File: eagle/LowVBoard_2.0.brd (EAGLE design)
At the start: 113 x 45.7 mm, 33 parts, among them IC1 ATMEGA328P-PU, IC2 MCP7940M, IC3 SN74HC595, IC4 SN74HC595, J1 CONNJACKR/APCB5.5X2.1MM, Q1 16MHz, Q2 32.768kHz

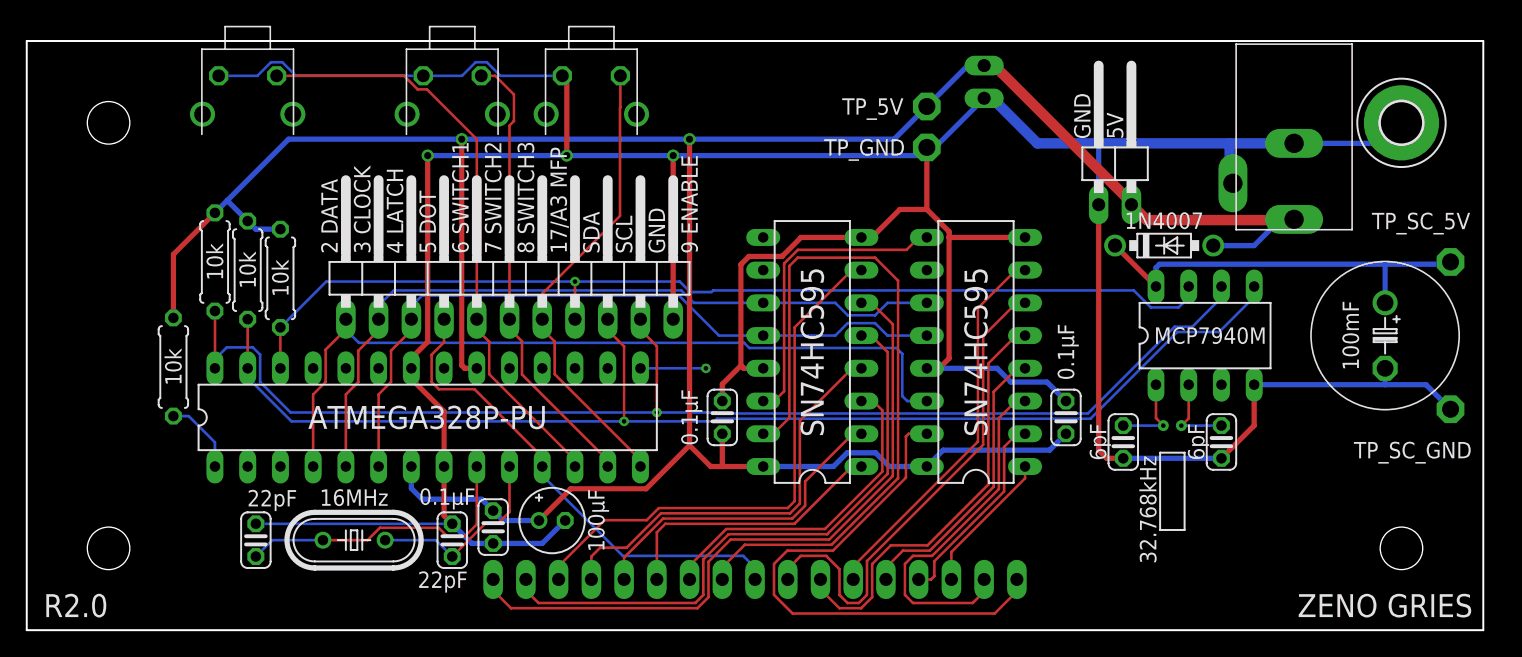
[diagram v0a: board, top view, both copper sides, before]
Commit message: added clearance for wodden board in front of switches and jack
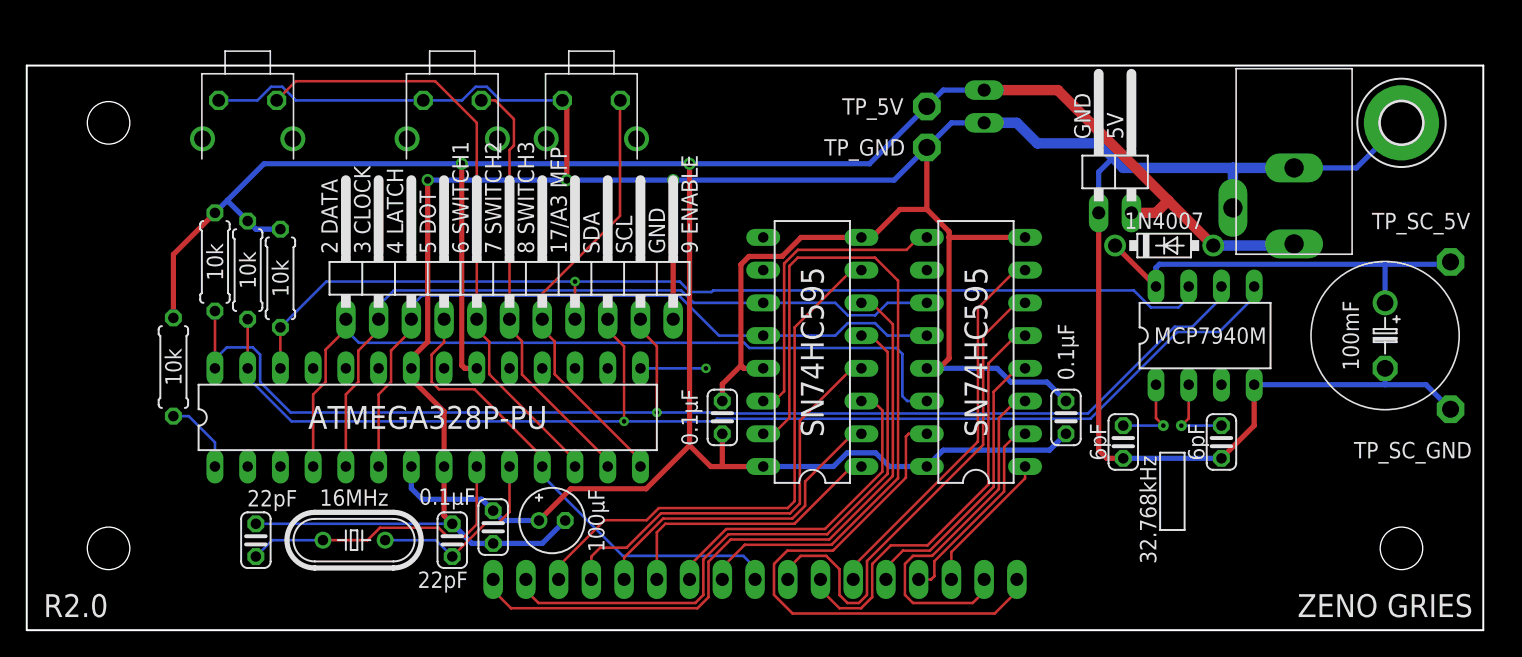
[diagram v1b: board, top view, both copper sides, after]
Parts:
- moved J1 1.91 mm to (98.3, 36.4)
- moved POWER 1.91 mm to (74.3, 40.6)
- moved S1 1.91 mm to (17.1, 39.6)
- moved S2 1.91 mm to (33.0, 39.6)
- moved S3 1.91 mm to (43.8, 39.6)
- moved POWER_D 0.63 mm to (84.5, 36.2)
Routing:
- net +5V: track 218.9 -> 210.4 mm
- net GND: track 309.7 -> 305.9 mm
- net SWITCH3: track 36.0 -> 34.1 mm
- net SWITCH2: track 35.3 -> 33.4 mm
- net SWITCH1: track 46.1 -> 47.3 mm
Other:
- board size 113 x 45.7 mm -> 113 x 43.8 mm
